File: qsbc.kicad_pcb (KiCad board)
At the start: 6 copper layers, 80 x 80 mm, 2 parts, among them U1 MIMX8MN5DVPIZAA, U3 MT40A1G16KD-062E

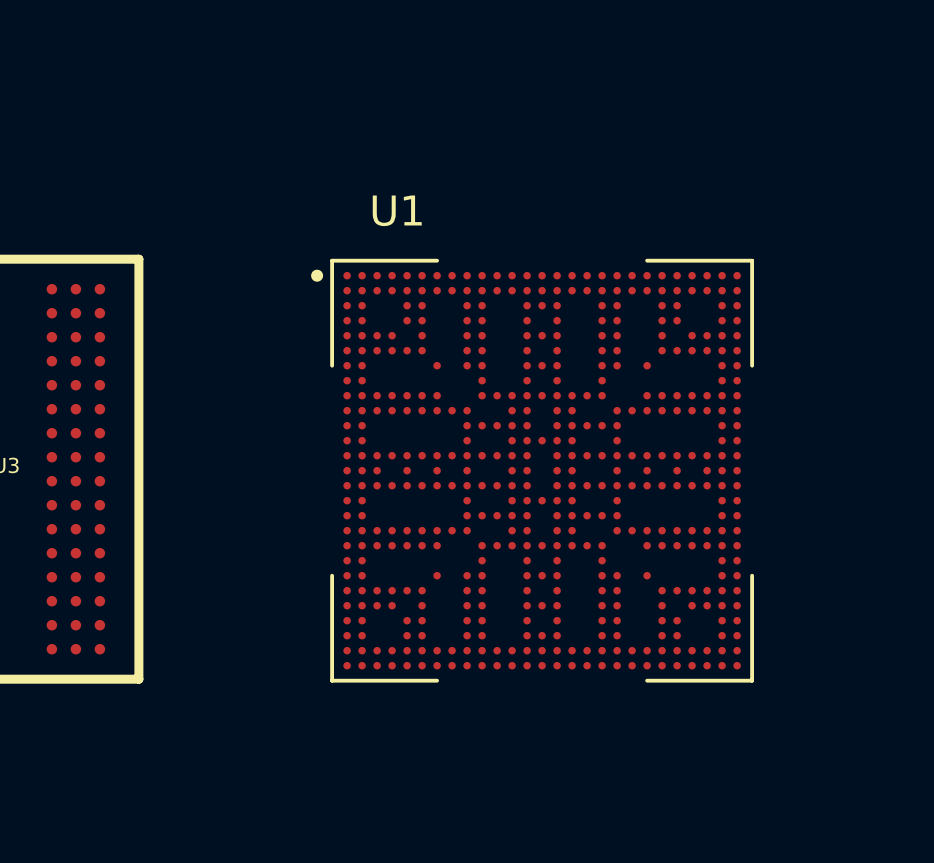
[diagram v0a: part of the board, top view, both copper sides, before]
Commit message: move to i.MX8M Mini
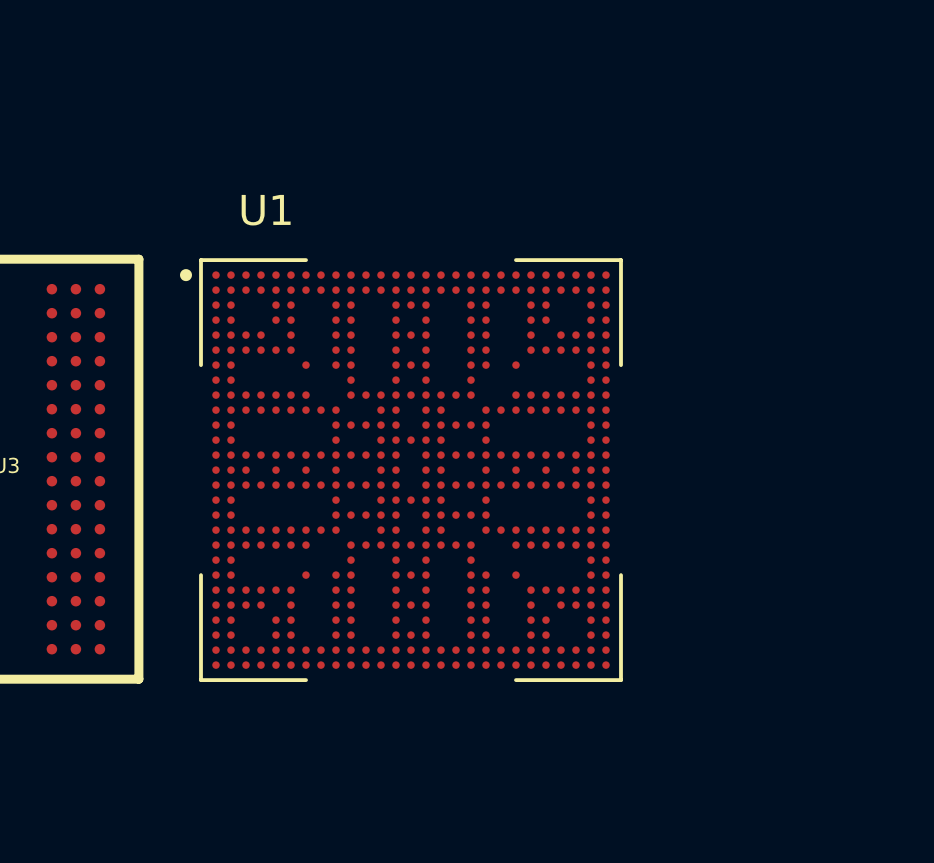
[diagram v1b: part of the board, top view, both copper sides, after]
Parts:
- U1: value MIMX8MN5DVPIZAA -> MIMX8MN5DVTJZAA
- moved U1 4.37 mm to (180.6, 105.0)
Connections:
- U1 pad A1: GND -> unconnected-(U1-PadA1)
- U1 pad A19: unconnected-(U1-PadA19) -> (no net)
- U1 pad A2: /DDR/DRAM_D01 -> unconnected-(U1-PadA2)
- U1 pad A20: unconnected-(U1-PadA20) -> (no net)
- U1 pad A21: GND -> (no net)
- U1 pad A22: (no net) -> unconnected-(U1-PadA22)
- U1 pad A23: (no net) -> unconnected-(U1-PadA23)
- U1 pad A24: (no net) -> unconnected-(U1-PadA24)
- U1 pad A25: (no net) -> unconnected-(U1-PadA25)
- U1 pad A26: (no net) -> unconnected-(U1-PadA26)
- U1 pad A27: (no net) -> unconnected-(U1-PadA27)
- U1 pad A3: /DDR/DRAM_D02 -> unconnected-(U1-PadA3)
- U1 pad AA1: GND -> unconnected-(U1-PadAA1)
- U1 pad AA2: /DDR/DRAM_A01 -> unconnected-(U1-PadAA2)
- U1 pad AA21: GND -> unconnected-(U1-PadAA21)
- U1 pad AA26: (no net) -> unconnected-(U1-PadAA26)
- U1 pad AA27: (no net) -> unconnected-(U1-PadAA27)
- U1 pad AB1: (no net) -> unconnected-(U1-PadAB1)
- U1 pad AB10: (no net) -> unconnected-(U1-PadAB10)
- U1 pad AB13: (no net) -> unconnected-(U1-PadAB13)
- U1 pad AB15: (no net) -> unconnected-(U1-PadAB15)
- U1 pad AB18: (no net) -> unconnected-(U1-PadAB18)
- U1 pad AB19: (no net) -> unconnected-(U1-PadAB19)
- U1 pad AB2: (no net) -> unconnected-(U1-PadAB2)
- U1 pad AB22: (no net) -> unconnected-(U1-PadAB22)
- U1 pad AB23: (no net) -> unconnected-(U1-PadAB23)
- U1 pad AB24: (no net) -> unconnected-(U1-PadAB24)
- U1 pad AB25: (no net) -> unconnected-(U1-PadAB25)
- U1 pad AB26: (no net) -> unconnected-(U1-PadAB26)
- U1 pad AB27: (no net) -> unconnected-(U1-PadAB27)
- U1 pad AB3: (no net) -> unconnected-(U1-PadAB3)
- U1 pad AB4: (no net) -> unconnected-(U1-PadAB4)
- U1 pad AB5: (no net) -> unconnected-(U1-PadAB5)
- U1 pad AB6: (no net) -> unconnected-(U1-PadAB6)
- U1 pad AB9: (no net) -> unconnected-(U1-PadAB9)
- U1 pad AC1: (no net) -> unconnected-(U1-PadAC1)
- U1 pad AC10: (no net) -> unconnected-(U1-PadAC10)
- U1 pad AC13: (no net) -> unconnected-(U1-PadAC13)
- U1 pad AC14: (no net) -> unconnected-(U1-PadAC14)
- U1 pad AC15: (no net) -> unconnected-(U1-PadAC15)
- U1 pad AC18: (no net) -> unconnected-(U1-PadAC18)
- U1 pad AC19: (no net) -> unconnected-(U1-PadAC19)
- U1 pad AC2: (no net) -> unconnected-(U1-PadAC2)
- U1 pad AC22: (no net) -> unconnected-(U1-PadAC22)
- U1 pad AC24: (no net) -> unconnected-(U1-PadAC24)
- U1 pad AC25: (no net) -> unconnected-(U1-PadAC25)
- U1 pad AC26: (no net) -> unconnected-(U1-PadAC26)
- U1 pad AC27: (no net) -> unconnected-(U1-PadAC27)
- U1 pad AC3: (no net) -> unconnected-(U1-PadAC3)
- U1 pad AC4: (no net) -> unconnected-(U1-PadAC4)
- U1 pad AC6: (no net) -> unconnected-(U1-PadAC6)
- U1 pad AC9: (no net) -> unconnected-(U1-PadAC9)
- U1 pad AD1: (no net) -> unconnected-(U1-PadAD1)
- U1 pad AD10: (no net) -> unconnected-(U1-PadAD10)
- U1 pad AD13: (no net) -> unconnected-(U1-PadAD13)
- U1 pad AD15: (no net) -> unconnected-(U1-PadAD15)
- U1 pad AD18: (no net) -> unconnected-(U1-PadAD18)
- U1 pad AD19: (no net) -> unconnected-(U1-PadAD19)
- U1 pad AD2: (no net) -> unconnected-(U1-PadAD2)
- U1 pad AD22: (no net) -> unconnected-(U1-PadAD22)
- U1 pad AD23: (no net) -> unconnected-(U1-PadAD23)
- U1 pad AD26: (no net) -> unconnected-(U1-PadAD26)
- U1 pad AD27: (no net) -> unconnected-(U1-PadAD27)
- U1 pad AD5: (no net) -> unconnected-(U1-PadAD5)
- U1 pad AD6: (no net) -> unconnected-(U1-PadAD6)
- U1 pad AD9: (no net) -> unconnected-(U1-PadAD9)
- U1 pad AE1: (no net) -> unconnected-(U1-PadAE1)
- U1 pad AE10: (no net) -> unconnected-(U1-PadAE10)
- U1 pad AE13: (no net) -> unconnected-(U1-PadAE13)
- U1 pad AE14: (no net) -> unconnected-(U1-PadAE14)
- U1 pad AE15: (no net) -> unconnected-(U1-PadAE15)
- U1 pad AE18: (no net) -> unconnected-(U1-PadAE18)
- U1 pad AE19: (no net) -> unconnected-(U1-PadAE19)
- U1 pad AE2: (no net) -> unconnected-(U1-PadAE2)
- U1 pad AE22: (no net) -> unconnected-(U1-PadAE22)
- U1 pad AE23: (no net) -> unconnected-(U1-PadAE23)
- U1 pad AE26: (no net) -> unconnected-(U1-PadAE26)
- U1 pad AE27: (no net) -> unconnected-(U1-PadAE27)
- U1 pad AE5: (no net) -> unconnected-(U1-PadAE5)
- U1 pad AE6: (no net) -> unconnected-(U1-PadAE6)
- U1 pad AE9: (no net) -> unconnected-(U1-PadAE9)
- U1 pad AF1: (no net) -> unconnected-(U1-PadAF1)
- U1 pad AF10: (no net) -> unconnected-(U1-PadAF10)
- U1 pad AF11: (no net) -> unconnected-(U1-PadAF11)
- U1 pad AF12: (no net) -> unconnected-(U1-PadAF12)
- U1 pad AF13: (no net) -> unconnected-(U1-PadAF13)
- U1 pad AF14: (no net) -> unconnected-(U1-PadAF14)
- U1 pad AF15: (no net) -> unconnected-(U1-PadAF15)
- U1 pad AF16: (no net) -> unconnected-(U1-PadAF16)
- U1 pad AF17: (no net) -> unconnected-(U1-PadAF17)
- U1 pad AF18: (no net) -> unconnected-(U1-PadAF18)
- U1 pad AF19: (no net) -> unconnected-(U1-PadAF19)
- U1 pad AF2: (no net) -> unconnected-(U1-PadAF2)
- U1 pad AF20: (no net) -> unconnected-(U1-PadAF20)
- U1 pad AF21: (no net) -> unconnected-(U1-PadAF21)
- U1 pad AF22: (no net) -> unconnected-(U1-PadAF22)
- U1 pad AF23: (no net) -> unconnected-(U1-PadAF23)
- U1 pad AF24: (no net) -> unconnected-(U1-PadAF24)
- U1 pad AF25: (no net) -> unconnected-(U1-PadAF25)
- U1 pad AF26: (no net) -> unconnected-(U1-PadAF26)
- U1 pad AF27: (no net) -> unconnected-(U1-PadAF27)
- U1 pad AF3: (no net) -> unconnected-(U1-PadAF3)
- U1 pad AF4: (no net) -> unconnected-(U1-PadAF4)
- U1 pad AF5: (no net) -> unconnected-(U1-PadAF5)
- U1 pad AF6: (no net) -> unconnected-(U1-PadAF6)
- U1 pad AF7: (no net) -> unconnected-(U1-PadAF7)
- U1 pad AF8: (no net) -> unconnected-(U1-PadAF8)
- U1 pad AF9: (no net) -> unconnected-(U1-PadAF9)
- U1 pad AG1: (no net) -> unconnected-(U1-PadAG1)
- U1 pad AG10: (no net) -> unconnected-(U1-PadAG10)
- U1 pad AG11: (no net) -> unconnected-(U1-PadAG11)
- U1 pad AG12: (no net) -> unconnected-(U1-PadAG12)
- U1 pad AG13: (no net) -> unconnected-(U1-PadAG13)
- U1 pad AG14: (no net) -> unconnected-(U1-PadAG14)
- U1 pad AG15: (no net) -> unconnected-(U1-PadAG15)
- U1 pad AG16: (no net) -> unconnected-(U1-PadAG16)
- U1 pad AG17: (no net) -> unconnected-(U1-PadAG17)
- U1 pad AG18: (no net) -> unconnected-(U1-PadAG18)
- U1 pad AG19: (no net) -> unconnected-(U1-PadAG19)
- U1 pad AG2: (no net) -> unconnected-(U1-PadAG2)
- U1 pad AG20: (no net) -> unconnected-(U1-PadAG20)
- U1 pad AG21: (no net) -> unconnected-(U1-PadAG21)
- U1 pad AG22: (no net) -> unconnected-(U1-PadAG22)
- U1 pad AG23: (no net) -> unconnected-(U1-PadAG23)
- U1 pad AG24: (no net) -> unconnected-(U1-PadAG24)
- U1 pad AG25: (no net) -> unconnected-(U1-PadAG25)
- U1 pad AG26: (no net) -> unconnected-(U1-PadAG26)
- U1 pad AG27: (no net) -> unconnected-(U1-PadAG27)
- U1 pad AG3: (no net) -> unconnected-(U1-PadAG3)
- U1 pad AG4: (no net) -> unconnected-(U1-PadAG4)
- U1 pad AG5: (no net) -> unconnected-(U1-PadAG5)
- U1 pad AG6: (no net) -> unconnected-(U1-PadAG6)
- U1 pad AG7: (no net) -> unconnected-(U1-PadAG7)
- U1 pad AG8: (no net) -> unconnected-(U1-PadAG8)
- U1 pad AG9: (no net) -> unconnected-(U1-PadAG9)
- U1 pad B1: /DDR/DRAM_DQS0_P -> unconnected-(U1-PadB1)
- U1 pad B19: unconnected-(U1-PadB19) -> (no net)
- U1 pad B2: /DDR/DRAM_DMI0 -> unconnected-(U1-PadB2)
- U1 pad B20: GND -> (no net)
- U1 pad B21: unconnected-(U1-PadB21) -> (no net)
- U1 pad B22: (no net) -> unconnected-(U1-PadB22)
- U1 pad B23: (no net) -> unconnected-(U1-PadB23)
- U1 pad B24: (no net) -> unconnected-(U1-PadB24)
- U1 pad B25: (no net) -> unconnected-(U1-PadB25)
- U1 pad B26: (no net) -> unconnected-(U1-PadB26)
- U1 pad B27: (no net) -> unconnected-(U1-PadB27)
- U1 pad B3: /DDR/DRAM_D00 -> unconnected-(U1-PadB3)
- U1 pad B4: /DDR/DRAM_D03 -> unconnected-(U1-PadB4)
- U1 pad C1: /DDR/DRAM_D06 -> unconnected-(U1-PadC1)
- U1 pad C10: GND -> unconnected-(U1-PadC10)
- U1 pad C13: (no net) -> unconnected-(U1-PadC13)
- U1 pad C14: GND -> unconnected-(U1-PadC14)
- U1 pad C15: (no net) -> unconnected-(U1-PadC15)
- U1 pad C18: GND -> unconnected-(U1-PadC18)
- U1 pad C19: (no net) -> unconnected-(U1-PadC19)
- U1 pad C2: /DDR/DRAM_DQS0_N -> unconnected-(U1-PadC2)
- U1 pad C22: (no net) -> unconnected-(U1-PadC22)
- U1 pad C23: (no net) -> unconnected-(U1-PadC23)
- U1 pad C26: (no net) -> unconnected-(U1-PadC26)
- U1 pad C27: (no net) -> unconnected-(U1-PadC27)
- U1 pad C5: (no net) -> unconnected-(U1-PadC5)
- U1 pad C6: GND -> unconnected-(U1-PadC6)
- U1 pad C9: (no net) -> unconnected-(U1-PadC9)
- U1 pad D1: /DDR/DRAM_D05 -> unconnected-(U1-PadD1)
- U1 pad D13: (no net) -> unconnected-(U1-PadD13)
- U1 pad D15: (no net) -> unconnected-(U1-PadD15)
- U1 pad D2: /DDR/DRAM_D07 -> unconnected-(U1-PadD2)
- U1 pad D22: (no net) -> unconnected-(U1-PadD22)
- U1 pad D23: (no net) -> unconnected-(U1-PadD23)
- U1 pad D26: (no net) -> unconnected-(U1-PadD26)
- U1 pad D27: (no net) -> unconnected-(U1-PadD27)
- U1 pad D5: (no net) -> unconnected-(U1-PadD5)
- U1 pad D9: (no net) -> unconnected-(U1-PadD9)
- U1 pad E1: /DDR/DRAM_D15 -> unconnected-(U1-PadE1)
- U1 pad E13: (no net) -> unconnected-(U1-PadE13)
- U1 pad E15: (no net) -> unconnected-(U1-PadE15)
- U1 pad E19: GND -> unconnected-(U1-PadE19)
- U1 pad E2: /DDR/DRAM_D04 -> unconnected-(U1-PadE2)
- U1 pad E22: (no net) -> unconnected-(U1-PadE22)
- U1 pad E24: (no net) -> unconnected-(U1-PadE24)
- U1 pad E25: (no net) -> unconnected-(U1-PadE25)
- U1 pad E26: (no net) -> unconnected-(U1-PadE26)
- U1 pad E27: (no net) -> unconnected-(U1-PadE27)
- U1 pad E3: GND -> unconnected-(U1-PadE3)
- U1 pad E4: /DDR/DRAM_A09 -> unconnected-(U1-PadE4)
- U1 pad E9: (no net) -> unconnected-(U1-PadE9)
- U1 pad F1: /DDR/DRAM_DQS1_N -> unconnected-(U1-PadF1)
- U1 pad F13: (no net) -> unconnected-(U1-PadF13)
- U1 pad F15: (no net) -> unconnected-(U1-PadF15)
- U1 pad F18: (no net) -> unconnected-(U1-PadF18)
- U1 pad F19: (no net) -> unconnected-(U1-PadF19)
- U1 pad F2: /DDR/DRAM_D14 -> unconnected-(U1-PadF2)
- U1 pad F22: (no net) -> unconnected-(U1-PadF22)
- U1 pad F23: (no net) -> unconnected-(U1-PadF23)
- U1 pad F24: (no net) -> unconnected-(U1-PadF24)
- U1 pad F25: (no net) -> unconnected-(U1-PadF25)
- U1 pad F26: (no net) -> unconnected-(U1-PadF26)
- U1 pad F27: (no net) -> unconnected-(U1-PadF27)
- U1 pad F3: (no net) -> unconnected-(U1-PadF3)
- U1 pad F4: (no net) -> unconnected-(U1-PadF4)
- U1 pad F5: (no net) -> unconnected-(U1-PadF5)
- U1 pad F9: (no net) -> unconnected-(U1-PadF9)
- U1 pad G1: /DDR/DRAM_D08 -> unconnected-(U1-PadG1)
- U1 pad G13: (no net) -> unconnected-(U1-PadG13)
- U1 pad G15: (no net) -> unconnected-(U1-PadG15)
- U1 pad G19: GND -> unconnected-(U1-PadG19)
- U1 pad G2: /DDR/DRAM_DQS1_P -> unconnected-(U1-PadG2)
- U1 pad G26: (no net) -> unconnected-(U1-PadG26)
- U1 pad G27: (no net) -> unconnected-(U1-PadG27)
- U1 pad G7: (no net) -> unconnected-(U1-PadG7)
- U1 pad G9: (no net) -> unconnected-(U1-PadG9)
- U1 pad H1: /DDR/DRAM_D09 -> unconnected-(U1-PadH1)
- U1 pad H10: GND -> unconnected-(U1-PadH10)
- U1 pad H13: (no net) -> unconnected-(U1-PadH13)
- U1 pad H15: (no net) -> unconnected-(U1-PadH15)
- U1 pad H18: (no net) -> unconnected-(U1-PadH18)
- U1 pad H2: /DDR/DRAM_DMI1 -> unconnected-(U1-PadH2)
- U1 pad H26: (no net) -> unconnected-(U1-PadH26)
- U1 pad H27: (no net) -> unconnected-(U1-PadH27)
- U1 pad J1: /DDR/DRAM_D10 -> unconnected-(U1-PadJ1)
- U1 pad J10: /i.MX8MN Power/VDD_SOC -> unconnected-(U1-PadJ10)
- U1 pad J11: /i.MX8MN Power/VDD_SOC -> unconnected-(U1-PadJ11)
- U1 pad J12: /i.MX8MN Power/VDD_SOC -> unconnected-(U1-PadJ12)
- U1 pad J13: /i.MX8MN Power/VDD_SOC -> unconnected-(U1-PadJ13)
- U1 pad J14: GND -> unconnected-(U1-PadJ14)
- U1 pad J2: /DDR/DRAM_D11 -> unconnected-(U1-PadJ2)
- U1 pad J22: (no net) -> unconnected-(U1-PadJ22)
- U1 pad J23: (no net) -> unconnected-(U1-PadJ23)
- U1 pad J24: (no net) -> unconnected-(U1-PadJ24)
- U1 pad J25: (no net) -> unconnected-(U1-PadJ25)
- U1 pad J26: (no net) -> unconnected-(U1-PadJ26)
- U1 pad J27: (no net) -> unconnected-(U1-PadJ27)
- U1 pad J3: GND -> unconnected-(U1-PadJ3)
- U1 pad J4: /DDR/DRAM_CK_P -> unconnected-(U1-PadJ4)
- U1 pad J5: /DDR/DRAM_CK_N -> unconnected-(U1-PadJ5)
- U1 pad J6: /i.MX8MN Power/NVCC_DRAM -> unconnected-(U1-PadJ6)
- U1 pad J7: /i.MX8MN Power/NVCC_DRAM -> unconnected-(U1-PadJ7)
- U1 pad K1: /DDR/DRAM_D12 -> unconnected-(U1-PadK1)
- U1 pad K12: /i.MX8MN Power/VDD_SOC -> unconnected-(U1-PadK12)
- U1 pad K13: (no net) -> unconnected-(U1-PadK13)
- U1 pad K15: (no net) -> unconnected-(U1-PadK15)
- U1 pad K16: (no net) -> unconnected-(U1-PadK16)
- U1 pad K19: (no net) -> unconnected-(U1-PadK19)
- U1 pad K2: /DDR/DRAM_D13 -> unconnected-(U1-PadK2)
- U1 pad K22: (no net) -> unconnected-(U1-PadK22)
- U1 pad K23: (no net) -> unconnected-(U1-PadK23)
- U1 pad K24: (no net) -> unconnected-(U1-PadK24)
- U1 pad K25: (no net) -> unconnected-(U1-PadK25)
- U1 pad K26: (no net) -> unconnected-(U1-PadK26)
- U1 pad K27: (no net) -> unconnected-(U1-PadK27)
- U1 pad K3: (no net) -> unconnected-(U1-PadK3)
- U1 pad K4: (no net) -> unconnected-(U1-PadK4)
- U1 pad K5: (no net) -> unconnected-(U1-PadK5)
- U1 pad K6: (no net) -> unconnected-(U1-PadK6)
- U1 pad K7: (no net) -> unconnected-(U1-PadK7)
- U1 pad K8: (no net) -> unconnected-(U1-PadK8)
- U1 pad K9: (no net) -> unconnected-(U1-PadK9)
- U1 pad L1: /DDR/DRAM_A06 -> unconnected-(U1-PadL1)
- U1 pad L10: /i.MX8MN Power/VDD_SOC -> unconnected-(U1-PadL10)
- U1 pad L11: (no net) -> unconnected-(U1-PadL11)
- U1 pad L12: /i.MX8MN Power/VDD_SOC -> unconnected-(U1-PadL12)
- U1 pad L13: /i.MX8MN Power/VDD_SOC -> unconnected-(U1-PadL13)
- U1 pad L19: GND -> unconnected-(U1-PadL19)
- U1 pad L2: /DDR/DRAM_A08 -> unconnected-(U1-PadL2)
- U1 pad L26: (no net) -> unconnected-(U1-PadL26)
- U1 pad L27: (no net) -> unconnected-(U1-PadL27)
- U1 pad L9: /i.MX8MN Power/VDD_SOC -> unconnected-(U1-PadL9)
- U1 pad M1: /DDR/DRAM_A05 -> unconnected-(U1-PadM1)
- U1 pad M12: /i.MX8MN Power/VDD_SOC -> unconnected-(U1-PadM12)
- U1 pad M13: (no net) -> unconnected-(U1-PadM13)
- U1 pad M14: (no net) -> unconnected-(U1-PadM14)
- U1 pad M15: (no net) -> unconnected-(U1-PadM15)
- U1 pad M16: (no net) -> unconnected-(U1-PadM16)
- U1 pad M19: (no net) -> unconnected-(U1-PadM19)
- U1 pad M2: /DDR/DRAM_A07 -> unconnected-(U1-PadM2)
- U1 pad M26: (no net) -> unconnected-(U1-PadM26)
- U1 pad M27: (no net) -> unconnected-(U1-PadM27)
- U1 pad M9: (no net) -> unconnected-(U1-PadM9)
- U1 pad N10: /i.MX8MN Power/VDD_SOC -> unconnected-(U1-PadN10)
- U1 pad N11: /i.MX8MN Power/VDD_SOC -> unconnected-(U1-PadN11)
- U1 pad N12: /i.MX8MN Power/VDD_SOC -> unconnected-(U1-PadN12)
- U1 pad N13: /i.MX8MN Power/VDD_SOC -> unconnected-(U1-PadN13)
- U1 pad N19: GND -> unconnected-(U1-PadN19)
- U1 pad N2: /DDR/DRAM_CS0_N -> unconnected-(U1-PadN2)
- U1 pad N22: (no net) -> unconnected-(U1-PadN22)
- U1 pad N23: (no net) -> unconnected-(U1-PadN23)
- U1 pad N24: (no net) -> unconnected-(U1-PadN24)
- U1 pad N25: (no net) -> unconnected-(U1-PadN25)
- U1 pad N26: (no net) -> unconnected-(U1-PadN26)
- U1 pad N27: (no net) -> unconnected-(U1-PadN27)
- U1 pad N3: GND -> unconnected-(U1-PadN3)
- U1 pad N4: /DDR/DRAM_RESET_N -> unconnected-(U1-PadN4)
- U1 pad N5: /DDR/DRAM_ALERT_N -> unconnected-(U1-PadN5)
- U1 pad N6: /i.MX8MN Power/NVCC_DRAM -> unconnected-(U1-PadN6)
- U1 pad N7: /i.MX8MN Power/NVCC_DRAM -> unconnected-(U1-PadN7)
- U1 pad N8: GND -> unconnected-(U1-PadN8)
- U1 pad N9: /i.MX8MN Power/VDD_SOC -> unconnected-(U1-PadN9)
- U1 pad P1: /DDR/DRAM_CKE -> unconnected-(U1-PadP1)
- U1 pad P12: GND -> unconnected-(U1-PadP12)
- U1 pad P13: (no net) -> unconnected-(U1-PadP13)
- U1 pad P15: (no net) -> unconnected-(U1-PadP15)
- U1 pad P16: (no net) -> unconnected-(U1-PadP16)
- U1 pad P19: (no net) -> unconnected-(U1-PadP19)
- U1 pad P23: (no net) -> unconnected-(U1-PadP23)
- U1 pad P25: (no net) -> unconnected-(U1-PadP25)
- U1 pad P26: (no net) -> unconnected-(U1-PadP26)
- U1 pad P27: (no net) -> unconnected-(U1-PadP27)
- U1 pad P3: (no net) -> unconnected-(U1-PadP3)
- U1 pad P5: (no net) -> unconnected-(U1-PadP5)
- U1 pad P7: (no net) -> unconnected-(U1-PadP7)
- U1 pad P9: (no net) -> unconnected-(U1-PadP9)
- U1 pad R1: /DDR/DRAM_A12 -> unconnected-(U1-PadR1)
- U1 pad R11: (no net) -> unconnected-(U1-PadR11)
- U1 pad R13: (no net) -> unconnected-(U1-PadR13)
- U1 pad R15: (no net) -> unconnected-(U1-PadR15)
- U1 pad R19: GND -> unconnected-(U1-PadR19)
- U1 pad R2: /DDR/DRAM_A11 -> unconnected-(U1-PadR2)
- U1 pad R22: (no net) -> unconnected-(U1-PadR22)
- U1 pad R23: (no net) -> unconnected-(U1-PadR23)
- U1 pad R24: (no net) -> unconnected-(U1-PadR24)
- U1 pad R25: (no net) -> unconnected-(U1-PadR25)
- U1 pad R26: (no net) -> unconnected-(U1-PadR26)
- U1 pad R27: (no net) -> unconnected-(U1-PadR27)
- U1 pad R3: GND -> unconnected-(U1-PadR3)
- U1 pad R6: /i.MX8MN Power/NVCC_DRAM -> unconnected-(U1-PadR6)
- U1 pad R7: (no net) -> unconnected-(U1-PadR7)
- U1 pad R9: (no net) -> unconnected-(U1-PadR9)
- U1 pad T13: (no net) -> unconnected-(U1-PadT13)
- U1 pad T15: (no net) -> unconnected-(U1-PadT15)
- U1 pad T19: (no net) -> unconnected-(U1-PadT19)
- U1 pad T26: (no net) -> unconnected-(U1-PadT26)
- U1 pad T27: (no net) -> unconnected-(U1-PadT27)
- U1 pad T9: (no net) -> unconnected-(U1-PadT9)
- U1 pad U1: /DDR/DRAM_ZN -> unconnected-(U1-PadU1)
- U1 pad U11: (no net) -> unconnected-(U1-PadU11)
- U1 pad U13: (no net) -> unconnected-(U1-PadU13)
- U1 pad U15: (no net) -> unconnected-(U1-PadU15)
- U1 pad U17: (no net) -> unconnected-(U1-PadU17)
- U1 pad U19: GND -> unconnected-(U1-PadU19)
- U1 pad U2: /DDR/DRAM_A15 -> unconnected-(U1-PadU2)
- U1 pad U26: (no net) -> unconnected-(U1-PadU26)
- U1 pad U27: (no net) -> unconnected-(U1-PadU27)
- U1 pad U9: (no net) -> unconnected-(U1-PadU9)
- U1 pad V1: /DDR/DRAM_ODT -> unconnected-(U1-PadV1)
- U1 pad V13: (no net) -> unconnected-(U1-PadV13)
- U1 pad V15: (no net) -> unconnected-(U1-PadV15)
- U1 pad V19: (no net) -> unconnected-(U1-PadV19)
- U1 pad V2: /DDR/DRAM_A14 -> unconnected-(U1-PadV2)
- U1 pad V22: (no net) -> unconnected-(U1-PadV22)
- U1 pad V23: (no net) -> unconnected-(U1-PadV23)
- U1 pad V24: (no net) -> unconnected-(U1-PadV24)
- U1 pad V25: (no net) -> unconnected-(U1-PadV25)
- U1 pad V26: (no net) -> unconnected-(U1-PadV26)
- U1 pad V27: (no net) -> unconnected-(U1-PadV27)
- U1 pad V3: (no net) -> unconnected-(U1-PadV3)
- U1 pad V4: /DDR/DRAM_BA0 -> unconnected-(U1-PadV4)
- U1 pad V5: (no net) -> unconnected-(U1-PadV5)
- U1 pad V7: (no net) -> unconnected-(U1-PadV7)
- U1 pad V9: (no net) -> unconnected-(U1-PadV9)
- U1 pad W1: /DDR/DRAM_A10 -> unconnected-(U1-PadW1)
- U1 pad W10: GND -> unconnected-(U1-PadW10)
- U1 pad W12: GND -> unconnected-(U1-PadW12)
- U1 pad W13: (no net) -> unconnected-(U1-PadW13)
- U1 pad W14: GND -> unconnected-(U1-PadW14)
- U1 pad W15: (no net) -> unconnected-(U1-PadW15)
- U1 pad W16: GND -> unconnected-(U1-PadW16)
- U1 pad W17: (no net) -> unconnected-(U1-PadW17)
- U1 pad W18: GND -> unconnected-(U1-PadW18)
- U1 pad W2: /DDR/DRAM_BA1 -> unconnected-(U1-PadW2)
- U1 pad W22: (no net) -> unconnected-(U1-PadW22)
- U1 pad W23: (no net) -> unconnected-(U1-PadW23)
- U1 pad W24: (no net) -> unconnected-(U1-PadW24)
- U1 pad W25: (no net) -> unconnected-(U1-PadW25)
- U1 pad W26: (no net) -> unconnected-(U1-PadW26)
- U1 pad W27: (no net) -> unconnected-(U1-PadW27)
- U1 pad W3: (no net) -> unconnected-(U1-PadW3)
- U1 pad W4: GND -> unconnected-(U1-PadW4)
- U1 pad W5: (no net) -> unconnected-(U1-PadW5)
- U1 pad W6: GND -> unconnected-(U1-PadW6)
- U1 pad W7: (no net) -> unconnected-(U1-PadW7)
- U1 pad Y1: /DDR/DRAM_A04 -> unconnected-(U1-PadY1)
- U1 pad Y2: /DDR/DRAM_A02 -> unconnected-(U1-PadY2)
- U1 pad Y26: (no net) -> unconnected-(U1-PadY26)
- U1 pad Y27: (no net) -> unconnected-(U1-PadY27)
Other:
- rule pad_to_mask_clearance: 0 -> 0.05

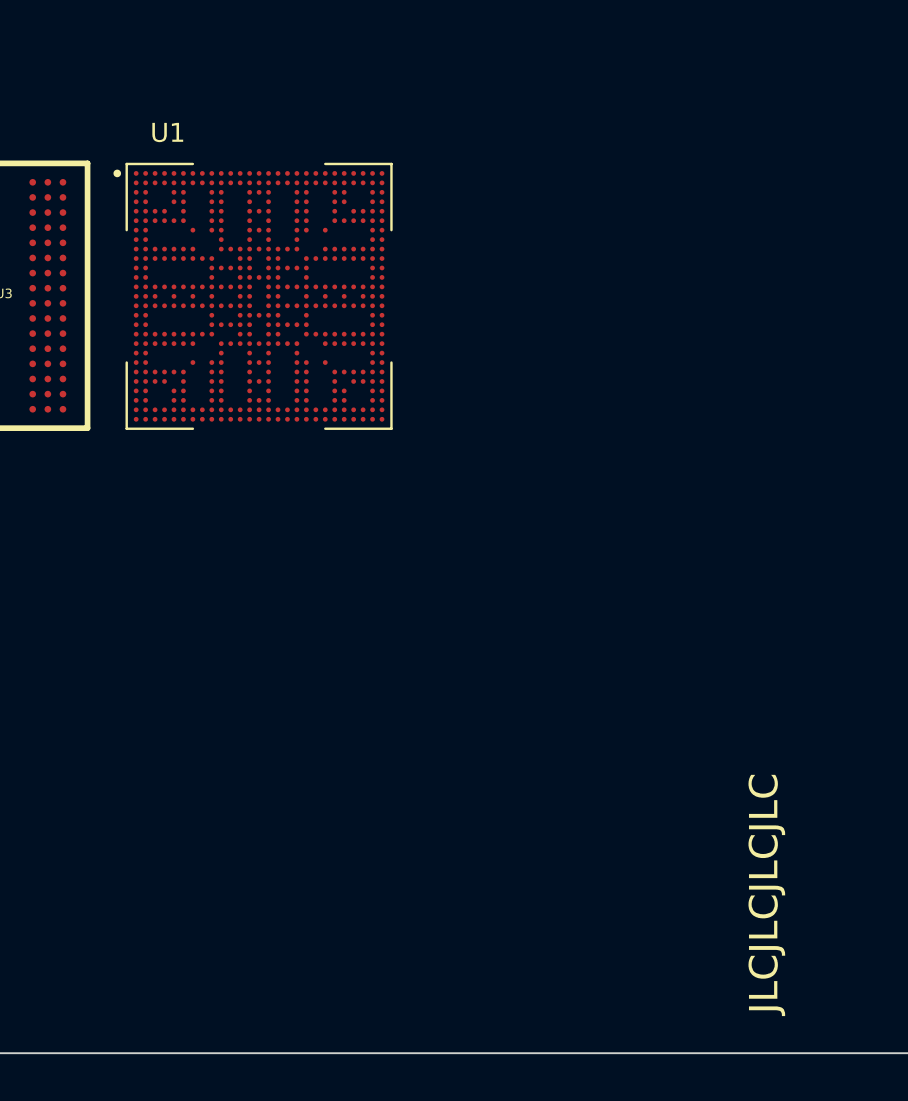
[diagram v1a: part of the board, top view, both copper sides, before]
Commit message: ddr sch done
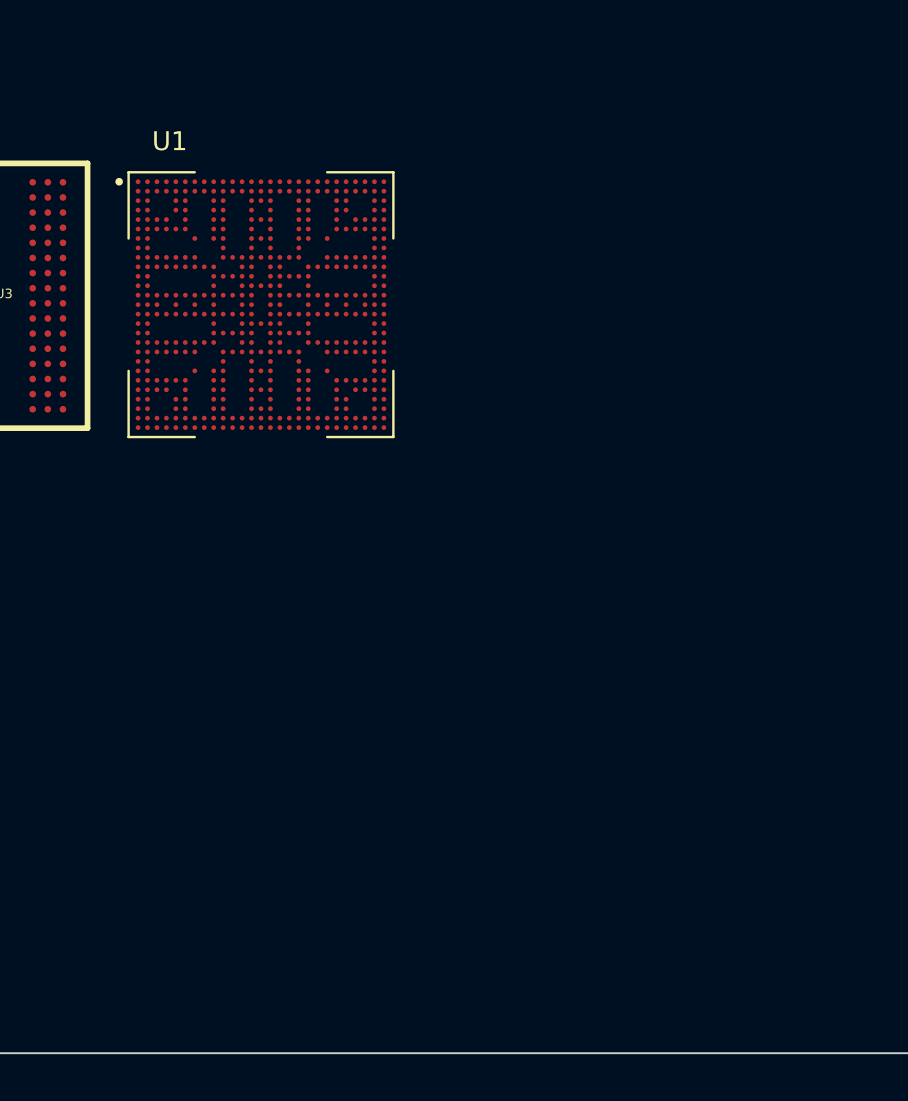
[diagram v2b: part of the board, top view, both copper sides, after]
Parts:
- U1: value MIMX8MN5DVTJZAA -> MIMX8MM6DVTLZAA
- moved U1 0.45 mm to (180.7, 105.4)
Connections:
- U1 pad A1: unconnected-(U1-PadA1) -> GND
- U1 pad A19: (no net) -> unconnected-(U1-PadA19)
- U1 pad A2: unconnected-(U1-PadA2) -> /DDR/DRAM_DQS0_P
- U1 pad A20: (no net) -> unconnected-(U1-PadA20)
- U1 pad A21: (no net) -> unconnected-(U1-PadA21)
- U1 pad A27: unconnected-(U1-PadA27) -> GND
- U1 pad A3: unconnected-(U1-PadA3) -> /DDR/DRAM_D06
- U1 pad A4: unconnected-(U1-PadA4) -> /DDR/DRAM_DMI0
- U1 pad A5: unconnected-(U1-PadA5) -> /DDR/DRAM_D00
- U1 pad AA10: unconnected-(U1-PadAA10) -> GND
- U1 pad AA13: unconnected-(U1-PadAA13) -> GND
- U1 pad AA15: unconnected-(U1-PadAA15) -> GND
- U1 pad AA18: unconnected-(U1-PadAA18) -> GND
- U1 pad AA19: unconnected-(U1-PadAA19) -> GND
- U1 pad AA21: unconnected-(U1-PadAA21) -> GND
- U1 pad AA7: unconnected-(U1-PadAA7) -> GND
- U1 pad AA9: unconnected-(U1-PadAA9) -> GND
- U1 pad AB25: unconnected-(U1-PadAB25) -> GND
- U1 pad AB3: unconnected-(U1-PadAB3) -> GND
- U1 pad AC25: unconnected-(U1-PadAC25) -> GND
- U1 pad AC3: unconnected-(U1-PadAC3) -> GND
- U1 pad AC4: unconnected-(U1-PadAC4) -> /DDR/DRAM_A10
- U1 pad AD5: unconnected-(U1-PadAD5) -> /DDR/DRAM_A00
- U1 pad AE10: unconnected-(U1-PadAE10) -> GND
- U1 pad AE13: unconnected-(U1-PadAE13) -> GND
- U1 pad AE14: unconnected-(U1-PadAE14) -> GND
- U1 pad AE15: unconnected-(U1-PadAE15) -> GND
- U1 pad AE18: unconnected-(U1-PadAE18) -> GND
- U1 pad AE19: unconnected-(U1-PadAE19) -> GND
- U1 pad AE2: unconnected-(U1-PadAE2) -> GND
- U1 pad AE22: unconnected-(U1-PadAE22) -> GND
- U1 pad AE23: unconnected-(U1-PadAE23) -> GND
- U1 pad AE5: unconnected-(U1-PadAE5) -> GND
- U1 pad AE6: unconnected-(U1-PadAE6) -> GND
- U1 pad AE9: unconnected-(U1-PadAE9) -> GND
- U1 pad AF3: unconnected-(U1-PadAF3) -> GND
- U1 pad AG1: unconnected-(U1-PadAG1) -> GND
- U1 pad AG27: unconnected-(U1-PadAG27) -> GND
- U1 pad B1: unconnected-(U1-PadB1) -> /DDR/DRAM_D05
- U1 pad B19: (no net) -> unconnected-(U1-PadB19)
- U1 pad B2: unconnected-(U1-PadB2) -> /DDR/DRAM_DQS0_N
- U1 pad B20: (no net) -> unconnected-(U1-PadB20)
- U1 pad B21: (no net) -> unconnected-(U1-PadB21)
- U1 pad B26: unconnected-(U1-PadB26) -> GND
- U1 pad B3: unconnected-(U1-PadB3) -> GND
- U1 pad B4: unconnected-(U1-PadB4) -> /DDR/DRAM_D07
- U1 pad B5: unconnected-(U1-PadB5) -> /DDR/DRAM_D01
- U1 pad C1: unconnected-(U1-PadC1) -> /DDR/DRAM_D04
- U1 pad C10: unconnected-(U1-PadC10) -> GND
- U1 pad C13: unconnected-(U1-PadC13) -> GND
- U1 pad C14: unconnected-(U1-PadC14) -> GND
- U1 pad C15: unconnected-(U1-PadC15) -> GND
- U1 pad C18: unconnected-(U1-PadC18) -> GND
- U1 pad C19: unconnected-(U1-PadC19) -> GND
- U1 pad C2: unconnected-(U1-PadC2) -> GND
- U1 pad C22: unconnected-(U1-PadC22) -> GND
- U1 pad C23: unconnected-(U1-PadC23) -> GND
- U1 pad C5: unconnected-(U1-PadC5) -> GND
- U1 pad C6: unconnected-(U1-PadC6) -> GND
- U1 pad C9: unconnected-(U1-PadC9) -> GND
- U1 pad D1: unconnected-(U1-PadD1) -> /DDR/DRAM_D03
- U1 pad D19: (no net) -> unconnected-(U1-PadD19)
- U1 pad D2: unconnected-(U1-PadD2) -> /DDR/DRAM_D02
- U1 pad D5: unconnected-(U1-PadD5) -> /DDR/DRAM_A08
- U1 pad E1: unconnected-(U1-PadE1) -> /DDR/DRAM_D14
- U1 pad E2: unconnected-(U1-PadE2) -> /DDR/DRAM_D15
- U1 pad E25: unconnected-(U1-PadE25) -> GND
- U1 pad E3: unconnected-(U1-PadE3) -> GND
- U1 pad E4: unconnected-(U1-PadE4) -> /DDR/DRAM_A07
- U1 pad F1: unconnected-(U1-PadF1) -> /DDR/DRAM_DMI1
- U1 pad F2: unconnected-(U1-PadF2) -> /DDR/DRAM_D08
- U1 pad F25: unconnected-(U1-PadF25) -> GND
- U1 pad F3: unconnected-(U1-PadF3) -> GND
- U1 pad F4: unconnected-(U1-PadF4) -> /DDR/DRAM_CKE
- U1 pad F6: unconnected-(U1-PadF6) -> /DDR/DRAM_ACT_N
- U1 pad G1: unconnected-(U1-PadG1) -> /DDR/DRAM_DQS1_P
- U1 pad G10: unconnected-(U1-PadG10) -> GND
- U1 pad G13: unconnected-(U1-PadG13) -> GND
- U1 pad G15: unconnected-(U1-PadG15) -> GND
- U1 pad G18: unconnected-(U1-PadG18) -> GND
- U1 pad G19: unconnected-(U1-PadG19) -> GND
- U1 pad G2: unconnected-(U1-PadG2) -> /DDR/DRAM_D09
- U1 pad G21: unconnected-(U1-PadG21) -> GND
- U1 pad G7: unconnected-(U1-PadG7) -> GND
- U1 pad G9: unconnected-(U1-PadG9) -> GND
- U1 pad H1: unconnected-(U1-PadH1) -> /DDR/DRAM_DQS1_N
- U1 pad H18: unconnected-(U1-PadH18) -> GND
- U1 pad H2: unconnected-(U1-PadH2) -> GND
- U1 pad J1: unconnected-(U1-PadJ1) -> /DDR/DRAM_D10
- U1 pad J2: unconnected-(U1-PadJ2) -> /DDR/DRAM_D11
- U1 pad J21: unconnected-(U1-PadJ21) -> GND
- U1 pad J25: unconnected-(U1-PadJ25) -> GND
- U1 pad J3: unconnected-(U1-PadJ3) -> GND
- U1 pad J5: unconnected-(U1-PadJ5) -> /DDR/DRAM_A09
- U1 pad J6: unconnected-(U1-PadJ6) -> /DDR/DRAM_A12
- U1 pad J7: unconnected-(U1-PadJ7) -> GND
- U1 pad K1: unconnected-(U1-PadK1) -> /DDR/DRAM_D13
- U1 pad K15: unconnected-(U1-PadK15) -> /i.MX8MM Power/NVCC_DRAM
- U1 pad K16: unconnected-(U1-PadK16) -> /i.MX8MM Power/NVCC_DRAM
- U1 pad K2: unconnected-(U1-PadK2) -> /DDR/DRAM_D12
- U1 pad K20: unconnected-(U1-PadK20) -> GND
- U1 pad K21: unconnected-(U1-PadK21) -> GND
- U1 pad K25: unconnected-(U1-PadK25) -> GND
- U1 pad K3: unconnected-(U1-PadK3) -> GND
- U1 pad K4: unconnected-(U1-PadK4) -> /DDR/DRAM_CS0_N
- U1 pad K5: unconnected-(U1-PadK5) -> /DDR/DRAM_A04
- U1 pad K6: unconnected-(U1-PadK6) -> /DDR/DRAM_A11
- U1 pad K7: unconnected-(U1-PadK7) -> GND
- U1 pad L12: unconnected-(U1-PadL12) -> GND
- U1 pad L15: unconnected-(U1-PadL15) -> /i.MX8MM Power/NVCC_DRAM
- U1 pad L16: unconnected-(U1-PadL16) -> GND
- U1 pad L2: unconnected-(U1-PadL2) -> /DDR/DRAM_BG0
- U1 pad M1: unconnected-(U1-PadM1) -> /DDR/DRAM_CK_P
- U1 pad M12: unconnected-(U1-PadM12) -> GND
- U1 pad M15: unconnected-(U1-PadM15) -> /i.MX8MM Power/NVCC_DRAM
- U1 pad M16: unconnected-(U1-PadM16) -> GND
- U1 pad M2: unconnected-(U1-PadM2) -> /DDR/DRAM_CK_N
- U1 pad N1: unconnected-(U1-PadN1) -> /DDR/DRAM_BA1
- U1 pad N12: unconnected-(U1-PadN12) -> GND
- U1 pad N15: unconnected-(U1-PadN15) -> /i.MX8MM Power/NVCC_DRAM
- U1 pad N16: unconnected-(U1-PadN16) -> GND
- U1 pad N18: unconnected-(U1-PadN18) -> /i.MX8MM Power/VDD_SOC
- U1 pad N2: unconnected-(U1-PadN2) -> /DDR/DRAM_MTEST
- U1 pad N21: unconnected-(U1-PadN21) -> GND
- U1 pad N25: unconnected-(U1-PadN25) -> GND
- U1 pad N3: unconnected-(U1-PadN3) -> GND
- U1 pad N4: unconnected-(U1-PadN4) -> /DDR/DRAM_A06
- U1 pad N5: unconnected-(U1-PadN5) -> /DDR/DRAM_A05
- U1 pad N6: unconnected-(U1-PadN6) -> /DDR/DRAM_A03
- U1 pad N7: unconnected-(U1-PadN7) -> GND
- U1 pad P1: unconnected-(U1-PadP1) -> /DDR/DRAM_VREF
- U1 pad P13: unconnected-(U1-PadP13) -> GND
- U1 pad P15: unconnected-(U1-PadP15) -> GND
- U1 pad P2: unconnected-(U1-PadP2) -> /DDR/DRAM_ZN
- U1 pad P21: unconnected-(U1-PadP21) -> GND
- U1 pad P25: unconnected-(U1-PadP25) -> GND
- U1 pad P3: unconnected-(U1-PadP3) -> GND
- U1 pad R1: unconnected-(U1-PadR1) -> /DDR/DRAM_RESET_N
- U1 pad R12: unconnected-(U1-PadR12) -> GND
- U1 pad R13: unconnected-(U1-PadR13) -> /i.MX8MM Power/VDD_SOC
- U1 pad R15: unconnected-(U1-PadR15) -> /i.MX8MM Power/VDD_SOC
- U1 pad R16: unconnected-(U1-PadR16) -> GND
- U1 pad R17: unconnected-(U1-PadR17) -> /i.MX8MM Power/NVCC_DRAM
- U1 pad R18: unconnected-(U1-PadR18) -> /i.MX8MM Power/VDD_SOC
- U1 pad R2: unconnected-(U1-PadR2) -> /DDR/DRAM_ALERT_N
- U1 pad R20: unconnected-(U1-PadR20) -> GND
- U1 pad R21: unconnected-(U1-PadR21) -> GND
- U1 pad R25: unconnected-(U1-PadR25) -> GND
- U1 pad R3: unconnected-(U1-PadR3) -> GND
- U1 pad R5: unconnected-(U1-PadR5) -> /DDR/DRAM_A15
- U1 pad R6: unconnected-(U1-PadR6) -> /DDR/DRAM_PARITY
- U1 pad R7: unconnected-(U1-PadR7) -> GND
- U1 pad T1: unconnected-(U1-PadT1) -> /DDR/DRAM_A14
- U1 pad T12: unconnected-(U1-PadT12) -> GND
- U1 pad T13: unconnected-(U1-PadT13) -> /i.MX8MM Power/VDD_SOC
- U1 pad T14: unconnected-(U1-PadT14) -> /i.MX8MM Power/VDD_SOC
- U1 pad T15: unconnected-(U1-PadT15) -> /i.MX8MM Power/VDD_SOC
- U1 pad T16: unconnected-(U1-PadT16) -> GND
- U1 pad T2: unconnected-(U1-PadT2) -> /DDR/DRAM_A16
- U1 pad U1: unconnected-(U1-PadU1) -> /DDR/DRAM_A01
- U1 pad U12: unconnected-(U1-PadU12) -> GND
- U1 pad U13: unconnected-(U1-PadU13) -> /i.MX8MM Power/VDD_SOC
- U1 pad U15: unconnected-(U1-PadU15) -> /i.MX8MM Power/VDD_SOC
- U1 pad U16: unconnected-(U1-PadU16) -> GND
- U1 pad U17: unconnected-(U1-PadU17) -> /i.MX8MM Power/NVCC_DRAM
- U1 pad U18: unconnected-(U1-PadU18) -> /i.MX8MM Power/VDD_SOC
- U1 pad U2: unconnected-(U1-PadU2) -> /DDR/DRAM_A02
- U1 pad V13: unconnected-(U1-PadV13) -> /i.MX8MM Power/VDD_SOC
- U1 pad V15: unconnected-(U1-PadV15) -> /i.MX8MM Power/VDD_SOC
- U1 pad V16: unconnected-(U1-PadV16) -> /i.MX8MM Power/VDD_SOC
- U1 pad V21: unconnected-(U1-PadV21) -> GND
- U1 pad V25: unconnected-(U1-PadV25) -> GND
- U1 pad V3: unconnected-(U1-PadV3) -> GND
- U1 pad V5: unconnected-(U1-PadV5) -> /DDR/DRAM_ODT
- U1 pad V6: unconnected-(U1-PadV6) -> /DDR/DRAM_BA0
- U1 pad V7: unconnected-(U1-PadV7) -> GND
- U1 pad W13: unconnected-(U1-PadW13) -> /i.MX8MM Power/VDD_SOC
- U1 pad W14: unconnected-(U1-PadW14) -> /i.MX8MM Power/VDD_SOC
- U1 pad W15: unconnected-(U1-PadW15) -> /i.MX8MM Power/VDD_SOC
- U1 pad W16: unconnected-(U1-PadW16) -> /i.MX8MM Power/VDD_SOC
- U1 pad W21: unconnected-(U1-PadW21) -> GND
- U1 pad W25: unconnected-(U1-PadW25) -> GND
- U1 pad W3: unconnected-(U1-PadW3) -> GND
- U1 pad W6: unconnected-(U1-PadW6) -> /DDR/DRAM_A13
- U1 pad W7: unconnected-(U1-PadW7) -> GND
- U1 pad Y13: unconnected-(U1-PadY13) -> GND
- U1 pad Y18: unconnected-(U1-PadY18) -> GND
- U1 pad Y2: unconnected-(U1-PadY2) -> GND
- U3 pad T3: unconnected-(U3-PadT3) -> /DDR/DRAM_PARITY
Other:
- board text added: "QSBC Rev 1.0 gitlab.com/quentin-z80/qsbc"
- board text removed: "JLCJLCJLCJLC"
- board text removed: "QSBC-ZERO Rev 2.0 gitlab.com/quentin-z80/qsbc"
